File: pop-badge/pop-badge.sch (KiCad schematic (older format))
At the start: 6 parts, among them J1 Conn_01x05, Q1 S9013, U26 Pico

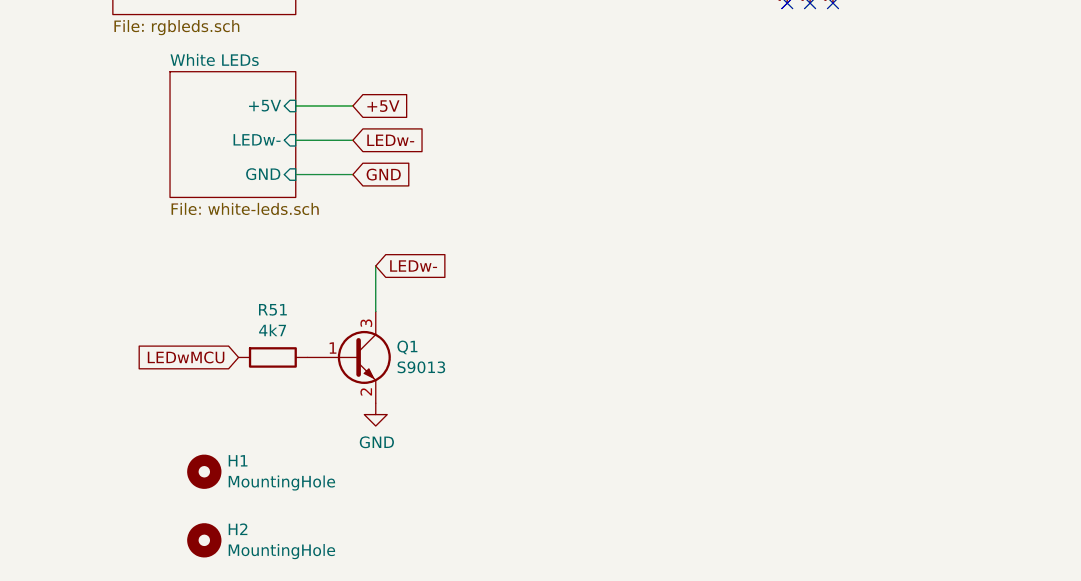
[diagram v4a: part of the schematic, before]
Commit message: add alternative path
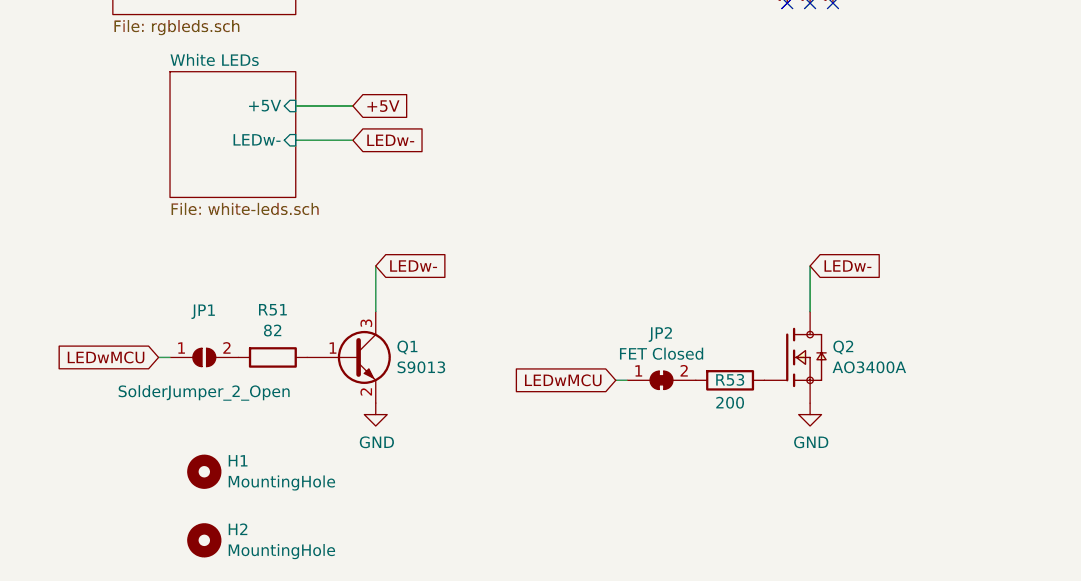
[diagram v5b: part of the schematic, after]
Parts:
- added JP1: SolderJumper_2_Open, Jumper:SolderJumper-2_P1.3mm_Open_Pad1.0x1.5mm, symbol Jumper:SolderJumper_2_Open
- added JP2: FET Closed, Jumper:SolderJumper-2_P1.3mm_Bridged_Pad1.0x1.5mm, symbol Jumper:SolderJumper_2_Bridged
- added Q2: AO3400A, footprints:SOT95P280X125-3N, symbol AO3400a:AO3400A
- added R53: 200, Resistor_SMD:R_0603_1608Metric_Pad1.05x0.95mm_HandSolder, symbol Device:R
- R51: value 4k7 -> 82
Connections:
- net GND: now also Q2.2
- net LEDw-: now also Q2.3
- net LEDwMCU: now also JP1.1 (A), JP2.1 (A); no longer R51.2
- new net: JP1.2 (B), R51.2
- new net: Q2.1, R53.1
- new net: JP2.2 (B), R53.2
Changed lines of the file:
@@
 Comment4 ""
 $EndDescr
-$Sheet
-S 1100 2350 800  650
-U 617DC867
-F0 "RGB LEDs" 50
-F1 "rgbleds.sch" 50
-F2 "+5V" I R 1900 2450 50
-F3 "GND" I R 1900 2850 50
-F4 "DIN" I R 1900 2650 50
-$EndSheet
 $Comp
 L Mechanical:MountingHole H1
@@
 F0 "White LEDs" 50
 F1 "white-leds.sch" 50
-F2 "GND" I R 1900 3700 50
-F3 "+5V" I R 1900 3400 50
-F4 "LEDw-" I R 1900 3550 50
+F2 "+5V" I R 1900 3400 50
+F3 "LEDw-" I R 1900 3550 50
 $EndSheet
 Wire Wire Line
@@
 Text GLabel 2150 3400 2    50   Input ~ 0
 +5V
-Text GLabel 1650 4500 0    50   Input ~ 0
-LEDwMCU
-Text GLabel 2150 3700 2    50   Input ~ 0
-GND
-Wire Wire Line
-	2150 3700 1900 3700
+Text GLabel 1300 4500 0    50   Input ~ 0
+LEDwMCU
 Wire Wire Line
 	1900 3550 2150 3550
@@
 Text GLabel 2100 2650 2    50   Input ~ 0
 DIN
-Text GLabel 2100 2850 2    50   Input ~ 0
-GND
 Wire Wire Line
 	2100 2450 1900 2450
 Wire Wire Line
 	1900 2650 2100 2650
-Wire Wire Line
-	2100 2850 1900 2850
 Text GLabel 3200 1050 0    50   Input ~ 0
 GND
@@
 AR Path="/61BDB595" Ref="R51"  Part="1"
 F 0 "R51" V 1593 4500 50  0000 C CNN
-F 1 "4k7" V 1684 4500 50  0000 C CNN
+F 1 "82" V 1684 4500 50  0000 C CNN
 F 2 "Resistor_SMD:R_0603_1608Metric_Pad1.05x0.95mm_HandSolder" V 1730 4500 50  0001 C CNN
 F 3 "~" H 1800 4500 50  0001 C CNN
@@
 Wire Wire Line
 	1200 1150 1400 1150
+Wire Wire Line
+	1300 4500 1350 4500
+$Comp
+L Jumper:SolderJumper_2_Open JP1
+U 1 1 6158AB24
+P 1500 4500
+F 0 "JP1" H 1500 4705 50  0000 C CNN
+F 1 "SolderJumper_2_Open" H 1500 4350 50  0000 C CNN
+F 2 "Jumper:SolderJumper-2_P1.3mm_Open_Pad1.0x1.5mm" H 1500 4500 50  0001 C CNN
+F 3 "~" H 1500 4500 50  0001 C CNN
+	1    1500 4500
+	1    0    0    -1
+$EndComp
+Text GLabel 3300 4600 0    50   Input ~ 0
+LEDwMCU
+$Comp
+L Device:R R?
+U 1 1 6158C467
+P 3800 4600
+AR Path="/615492B8/6158C467" Ref="R?"  Part="1"
+AR Path="/6158C467" Ref="R53"  Part="1"
+F 0 "R53" V 3800 4600 50  0000 C CNN
+F 1 "200" V 3900 4600 50  0000 C CNN
+F 2 "Resistor_SMD:R_0603_1608Metric_Pad1.05x0.95mm_HandSolder" V 3730 4600 50  0001 C CNN
+F 3 "~" H 3800 4600 50  0001 C CNN
+F 4 "0603" H 3800 4600 50  0001 C CNN "JLC"
+	1    3800 4600
+	0    1    1    0
+$EndComp
+Wire Wire Line
+	4150 4100 4150 4300
+$Comp
+L power:GND #PWR054
+U 1 1 6158C47D
+P 4150 4700
+F 0 "#PWR054" H 4150 4450 50  0001 C CNN
+F 1 "GND" H 4155 4527 50  0000 C CNN
+F 2 "" H 4150 4700 50  0001 C CNN
+F 3 "" H 4150 4700 50  0001 C CNN
+	1    4150 4700
+	1    0    0    -1
+$EndComp
+Text GLabel 4150 4100 2    50   Input ~ 0
+LEDw-
+Wire Wire Line
+	3300 4600 3350 4600
+$Comp
+L AO3400a:AO3400A Q2
+U 1 1 6158FC09
+P 4050 4500
+F 0 "Q2" H 4248 4546 50  0000 L CNN
+F 1 "AO3400A" H 4248 4455 50  0000 L CNN
+F 2 "footprints:SOT95P280X125-3N" H 4050 4500 50  0001 L BNN
+F 3 "" H 4050 4500 50  0001 L BNN
+F 4 "L" H 4050 4500 50  0001 L BNN "PARTREV"
+F 5 "IPC 7351B" H 4050 4500 50  0001 L BNN "STANDARD"
+F 6 "1.25 mm" H 4050 4500 50  0001 L BNN "MAXIMUM_PACKAGE_HEIGHT"
+F 7 "Alpha & Omega Semiconductor" H 4050 4500 50  0001 L BNN "MANUFACTURER"
+F 8 "C20917" H 4050 4500 50  0001 C CNN "JLC"
+	1    4050 4500
+	1    0    0    -1
+$EndComp
+$Comp
+L Jumper:SolderJumper_2_Bridged JP2
+U 1 1 61593252
+P 3500 4600
+F 0 "JP2" H 3500 4805 50  0000 C CNN
+F 1 "FET Closed" H 3500 4714 50  0000 C CNN
+F 2 "Jumper:SolderJumper-2_P1.3mm_Bridged_Pad1.0x1.5mm" H 3500 4600 50  0001 C CNN
+F 3 "~" H 3500 4600 50  0001 C CNN
+	1    3500 4600
+	1    0    0    -1
+$EndComp
+$Sheet
+S 1100 2350 800  650
+U 617DC867
+F0 "RGB LEDs" 50
+F1 "rgbleds.sch" 50
+F2 "+5V" I R 1900 2450 50
+F3 "GND" I R 1900 2850 50
+F4 "DIN" I R 1900 2650 50
+$EndSheet
+Wire Wire Line
+	2100 2850 1900 2850
+Text GLabel 2100 2850 2    50   Input ~ 0
+GND
 $EndSCHEMATC

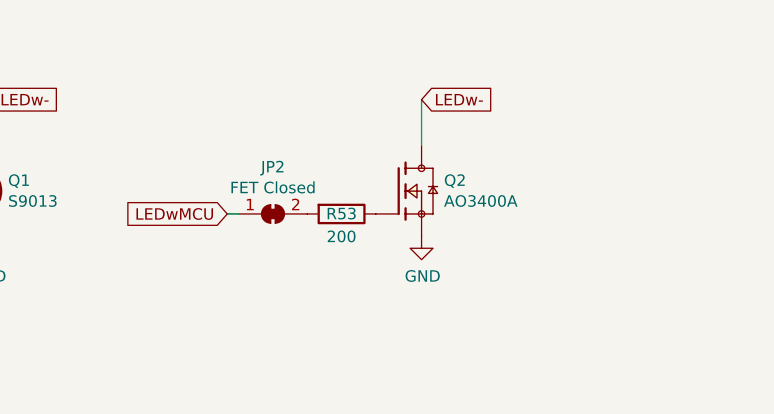
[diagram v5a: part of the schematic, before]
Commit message: add pull down for mosfet
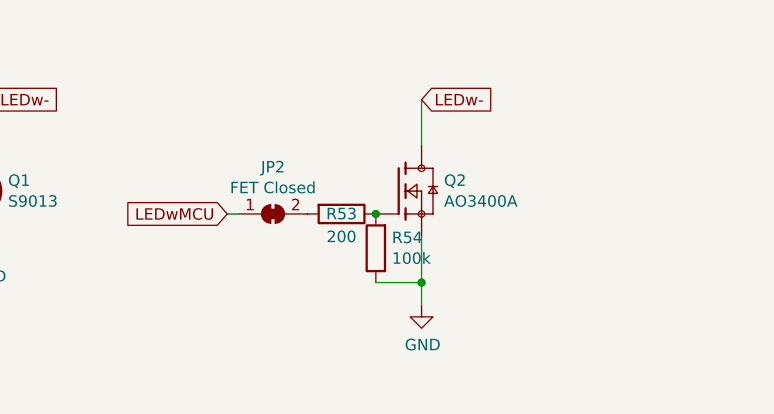
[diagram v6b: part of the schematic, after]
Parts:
- added R54: 100k, Resistor_SMD:R_0603_1608Metric_Pad1.05x0.95mm_HandSolder, symbol Device:R
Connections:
- net GND: now also R54.1
- net at Q2.1, R53.1: now also R54.2
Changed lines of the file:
@@
 L power:GND #PWR054
 U 1 1 6158C47D
-P 4150 4700
-F 0 "#PWR054" H 4150 4450 50  0001 C CNN
-F 1 "GND" H 4155 4527 50  0000 C CNN
-F 2 "" H 4150 4700 50  0001 C CNN
-F 3 "" H 4150 4700 50  0001 C CNN
-	1    4150 4700
+P 4150 5000
+F 0 "#PWR054" H 4150 4750 50  0001 C CNN
+F 1 "GND" H 4155 4827 50  0000 C CNN
+F 2 "" H 4150 5000 50  0001 C CNN
+F 3 "" H 4150 5000 50  0001 C CNN
+	1    4150 5000
 	1    0    0    -1
 $EndComp
@@
 Text GLabel 2100 2850 2    50   Input ~ 0
 GND
+$Comp
+L Device:R R54
+U 1 1 615C02CB
+P 3950 4750
+F 0 "R54" H 3880 4704 50  0000 R CNN
+F 1 "100k" H 3880 4795 50  0000 R CNN
+F 2 "Resistor_SMD:R_0603_1608Metric_Pad1.05x0.95mm_HandSolder" V 3880 4750 50  0001 C CNN
+F 3 "~" H 3950 4750 50  0001 C CNN
+F 4 "0603" H 3950 4750 50  0001 C CNN "JLC"
+	1    3950 4750
+	-1   0    0    1
+$EndComp
+Connection ~ 3950 4600
+Wire Wire Line
+	3950 4900 4150 4900
+Wire Wire Line
+	4150 4700 4150 4900
+Connection ~ 4150 4900
+Wire Wire Line
+	4150 4900 4150 5000
 $EndSCHEMATC

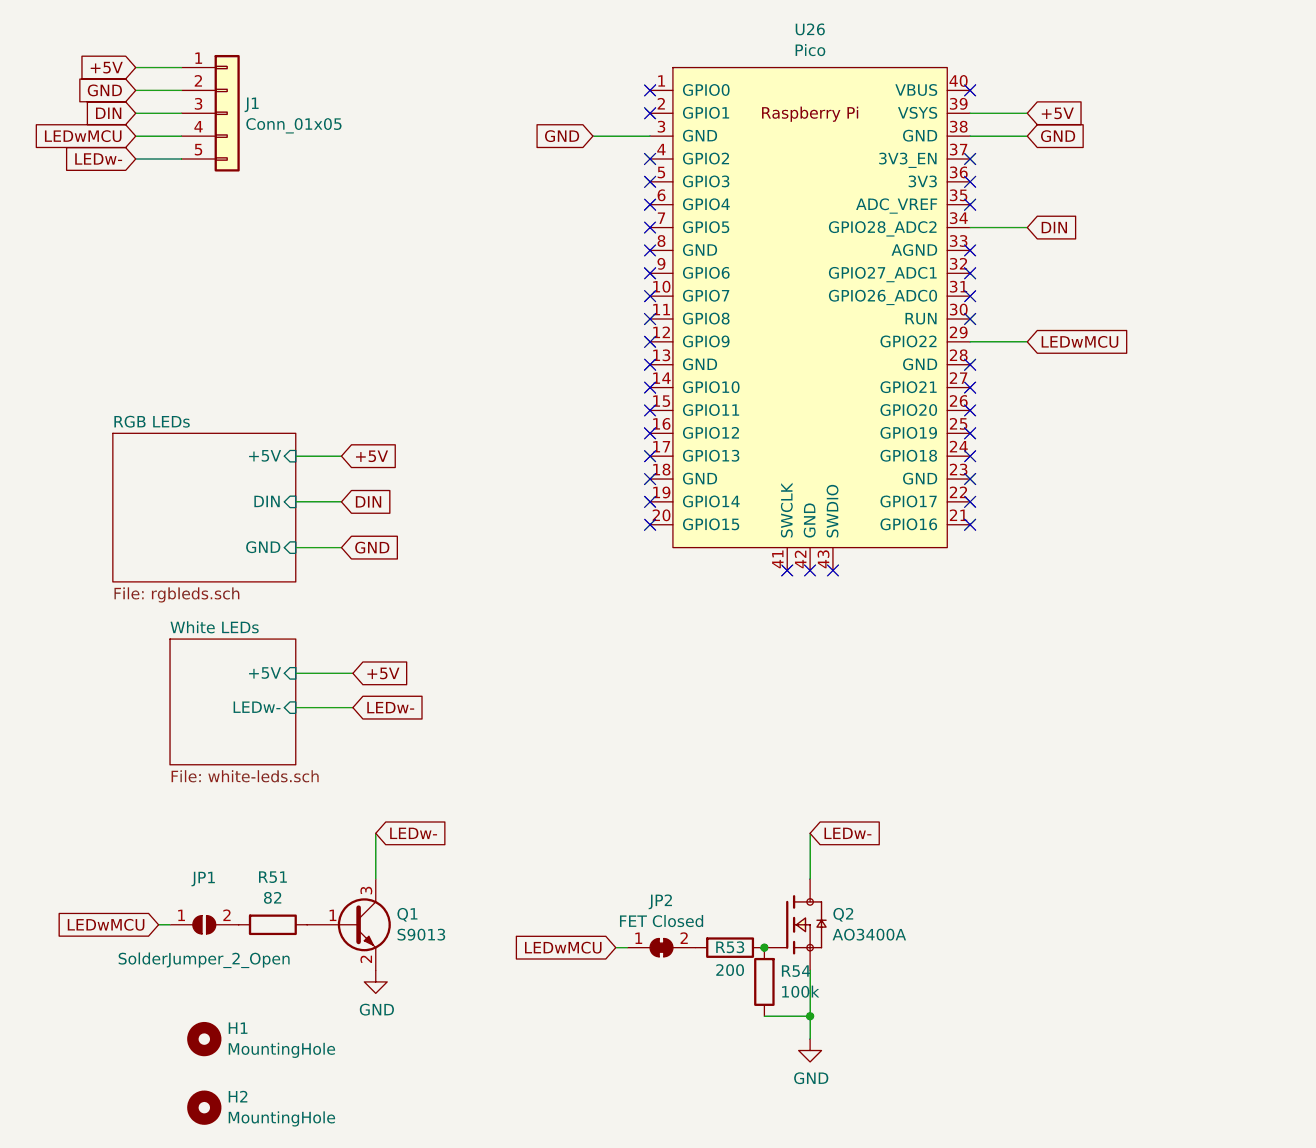
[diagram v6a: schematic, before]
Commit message: add button
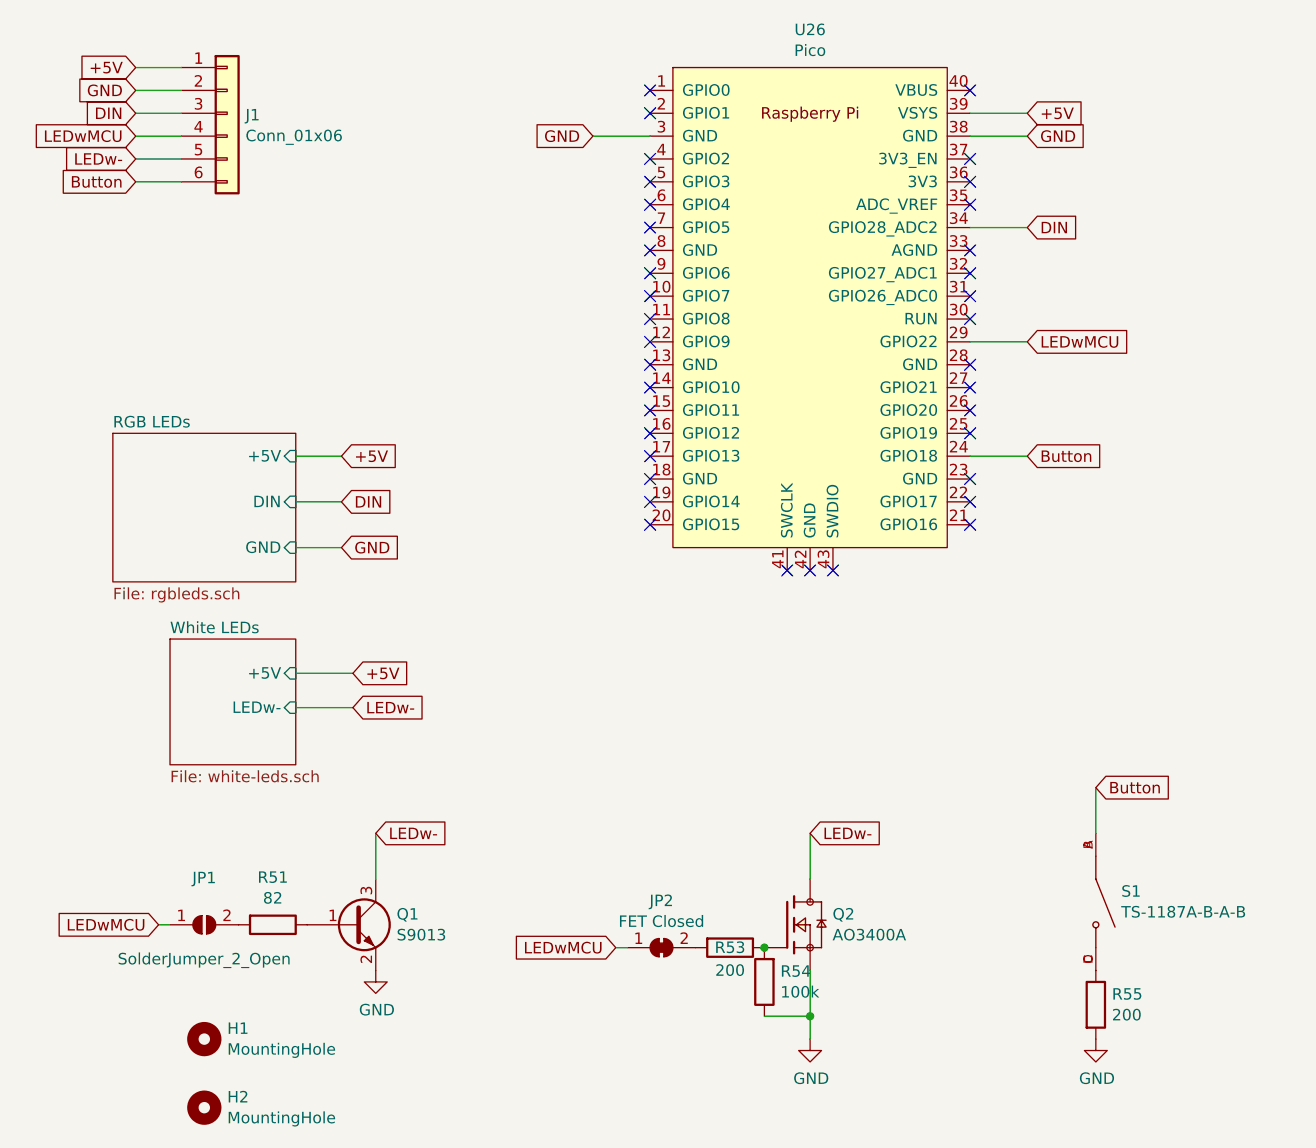
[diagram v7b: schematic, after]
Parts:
- removed J1: Conn_01x05, Connector_PinSocket_2.54mm:PinSocket_1x05_P2.54mm_Vertical, symbol Connector_Generic:Conn_01x05
- added J1: Conn_01x06, Connector_PinHeader_2.54mm:PinHeader_1x06_P2.54mm_Vertical, symbol Connector_Generic:Conn_01x06
- added R55: 200, Resistor_SMD:R_0603_1608Metric_Pad1.05x0.95mm_HandSolder, symbol Device:R
- added S1: TS-1187A-B-A-B, footprints:SW_TS-1187A-B-A-B, symbol TS-button:TS-1187A-B-A-B
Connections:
- net +5V: now also J1.1 (Pin_1)
- net DIN: now also J1.3 (Pin_3)
- net GND: now also J1.2 (Pin_2), R55.2
- net LEDw-: now also J1.5 (Pin_5)
- net LEDwMCU: now also J1.4 (Pin_4)
- net Button: now reaches U26.24 (GPIO18)
- net Button: now also J1.6 (Pin_6), S1.A, S1.B
- new net: R55.1, S1.C, S1.D
- no-connect marks 38 -> 37
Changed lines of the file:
@@
 NoConn ~ 4850 2650
 NoConn ~ 4850 2550
-NoConn ~ 4850 2450
+NoConn ~ 4850 2150
 NoConn ~ 4850 2350
 NoConn ~ 4850 2250
-NoConn ~ 4850 2150
 NoConn ~ 4850 2050
 NoConn ~ 4850 2750
@@
 Text GLabel 2250 4100 2    50   Input ~ 0
 LEDw-
-$Comp
-L Connector_Generic:Conn_01x05 J1
-U 1 1 61BFACBB
-P 1600 950
-F 0 "J1" H 1680 992 50  0000 L CNN
-F 1 "Conn_01x05" H 1680 901 50  0000 L CNN
-F 2 "Connector_PinSocket_2.54mm:PinSocket_1x05_P2.54mm_Vertical" H 1600 950 50  0001 C CNN
-F 3 "~" H 1600 950 50  0001 C CNN
-	1    1600 950
-	1    0    0    -1
-$EndComp
 Text GLabel 1200 1150 0    50   Input ~ 0
 LEDw-
@@
 Wire Wire Line
 	4150 4900 4150 5000
+Text GLabel 5400 3900 2    50   Input ~ 0
+Button
+$Comp
+L Device:R R55
+U 1 1 615CA836
+P 5400 4850
+F 0 "R55" H 5470 4896 50  0000 L CNN
+F 1 "200" H 5470 4805 50  0000 L CNN
+F 2 "Resistor_SMD:R_0603_1608Metric_Pad1.05x0.95mm_HandSolder" V 5330 4850 50  0001 C CNN
+F 3 "~" H 5400 4850 50  0001 C CNN
+	1    5400 4850
+	1    0    0    -1
+$EndComp
+$Comp
+L power:GND #PWR0103
+U 1 1 615CAE29
+P 5400 5000
+F 0 "#PWR0103" H 5400 4750 50  0001 C CNN
+F 1 "GND" H 5405 4827 50  0000 C CNN
+F 2 "" H 5400 5000 50  0001 C CNN
+F 3 "" H 5400 5000 50  0001 C CNN
+	1    5400 5000
+	1    0    0    -1
+$EndComp
+Wire Wire Line
+	5400 3900 5400 4100
+$Comp
+L Connector_Generic:Conn_01x06 J1
+U 1 1 615CEC6A
+P 1600 950
+F 0 "J1" H 1680 942 50  0000 L CNN
+F 1 "Conn_01x06" H 1680 851 50  0000 L CNN
+F 2 "Connector_PinHeader_2.54mm:PinHeader_1x06_P2.54mm_Vertical" H 1600 950 50  0001 C CNN
+F 3 "~" H 1600 950 50  0001 C CNN
+	1    1600 950
+	1    0    0    -1
+$EndComp
+Text GLabel 1200 1250 0    50   Input ~ 0
+Button
+Text GLabel 5100 2450 2    50   Input ~ 0
+Button
+Wire Wire Line
+	5100 2450 4850 2450
+Wire Wire Line
+	1400 1250 1200 1250
+$Comp
+L TS-button:TS-1187A-B-A-B S1
+U 1 1 615D35C1
+P 5400 4400
+F 0 "S1" V 5354 4511 50  0000 L CNN
+F 1 "TS-1187A-B-A-B" V 5445 4511 50  0000 L CNN
+F 2 "footprints:SW_TS-1187A-B-A-B" H 5400 4400 50  0001 L BNN
+F 3 "" H 5400 4400 50  0001 L BNN
+F 4 "A0" H 5400 4400 50  0001 L BNN "PARTREV"
+F 5 "XKB Industrial Precision" H 5400 4400 50  0001 L BNN "MANUFACTURER"
+F 6 "1.5mm" H 5400 4400 50  0001 L BNN "MAXIMUM_PACKAGE_HEIGHT"
+F 7 "Manufacturer Recommendations" H 5400 4400 50  0001 L BNN "STANDARD"
+F 8 "C318884" H 5400 4400 50  0001 C CNN "JLC"
+	1    5400 4400
+	0    1    1    0
+$EndComp
 $EndSCHEMATC

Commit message: some cosmetic changes
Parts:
- R55: JLC (none) -> 0603
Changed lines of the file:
@@
 F 2 "Resistor_SMD:R_0603_1608Metric_Pad1.05x0.95mm_HandSolder" V 5330 4850 50  0001 C CNN
 F 3 "~" H 5400 4850 50  0001 C CNN
+F 4 "0603" H 5400 4850 50  0001 C CNN "JLC"
 	1    5400 4850
 	1    0    0    -1
